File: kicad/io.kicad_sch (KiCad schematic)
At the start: 14 parts, among them P1 Mini-DIN_6pins_ver3, SW2 SW_DIP_x08, U6 74HC273, U8 74HC244

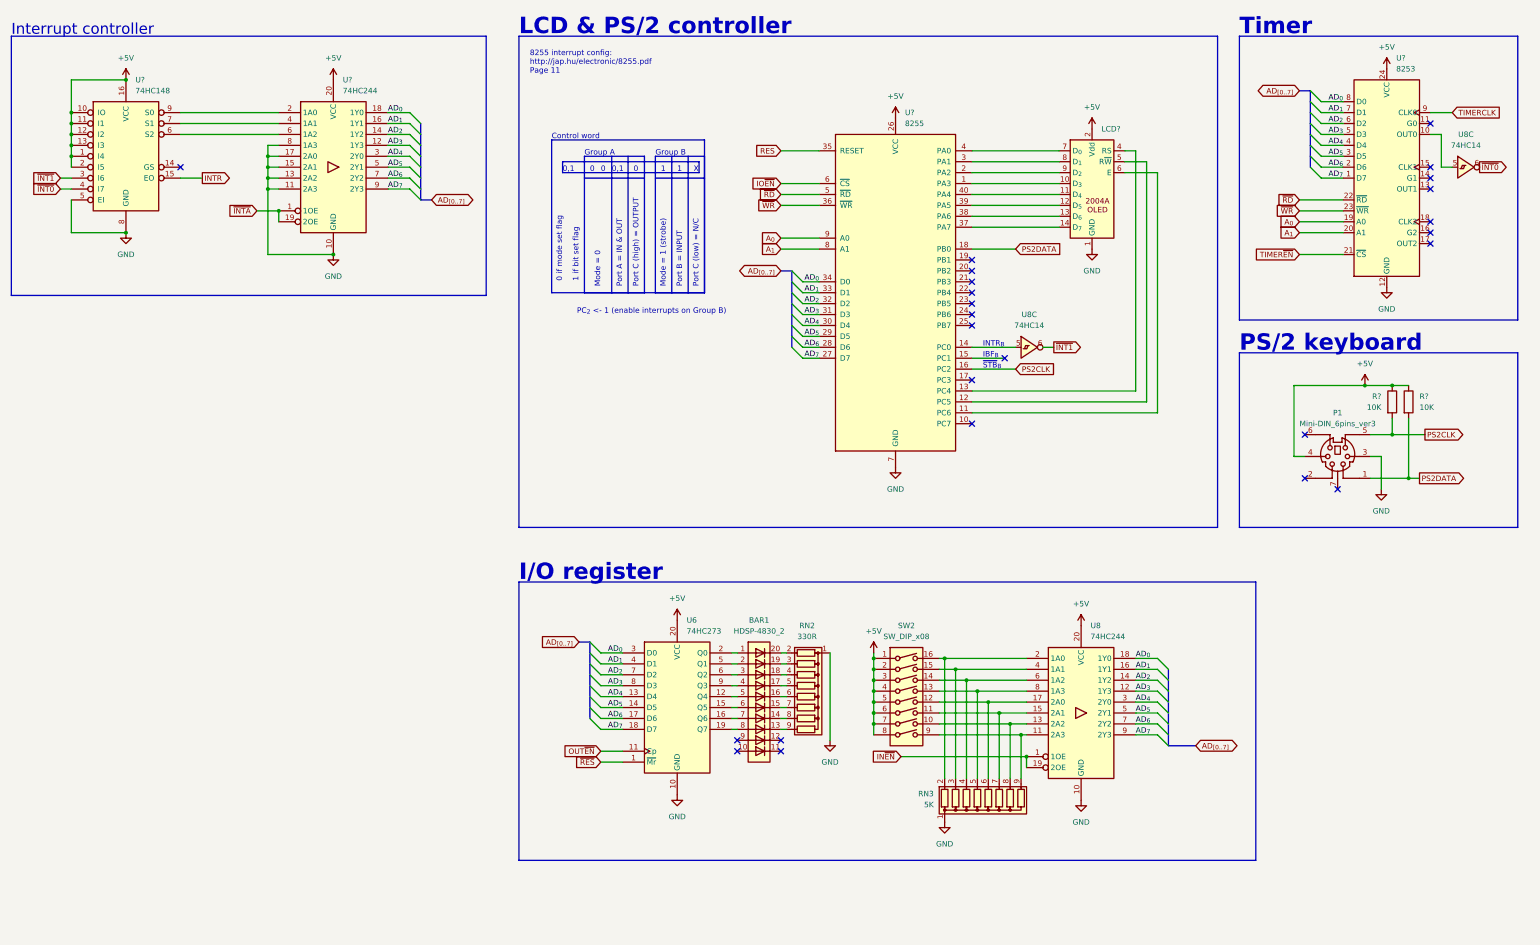
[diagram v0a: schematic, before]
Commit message: Add UART
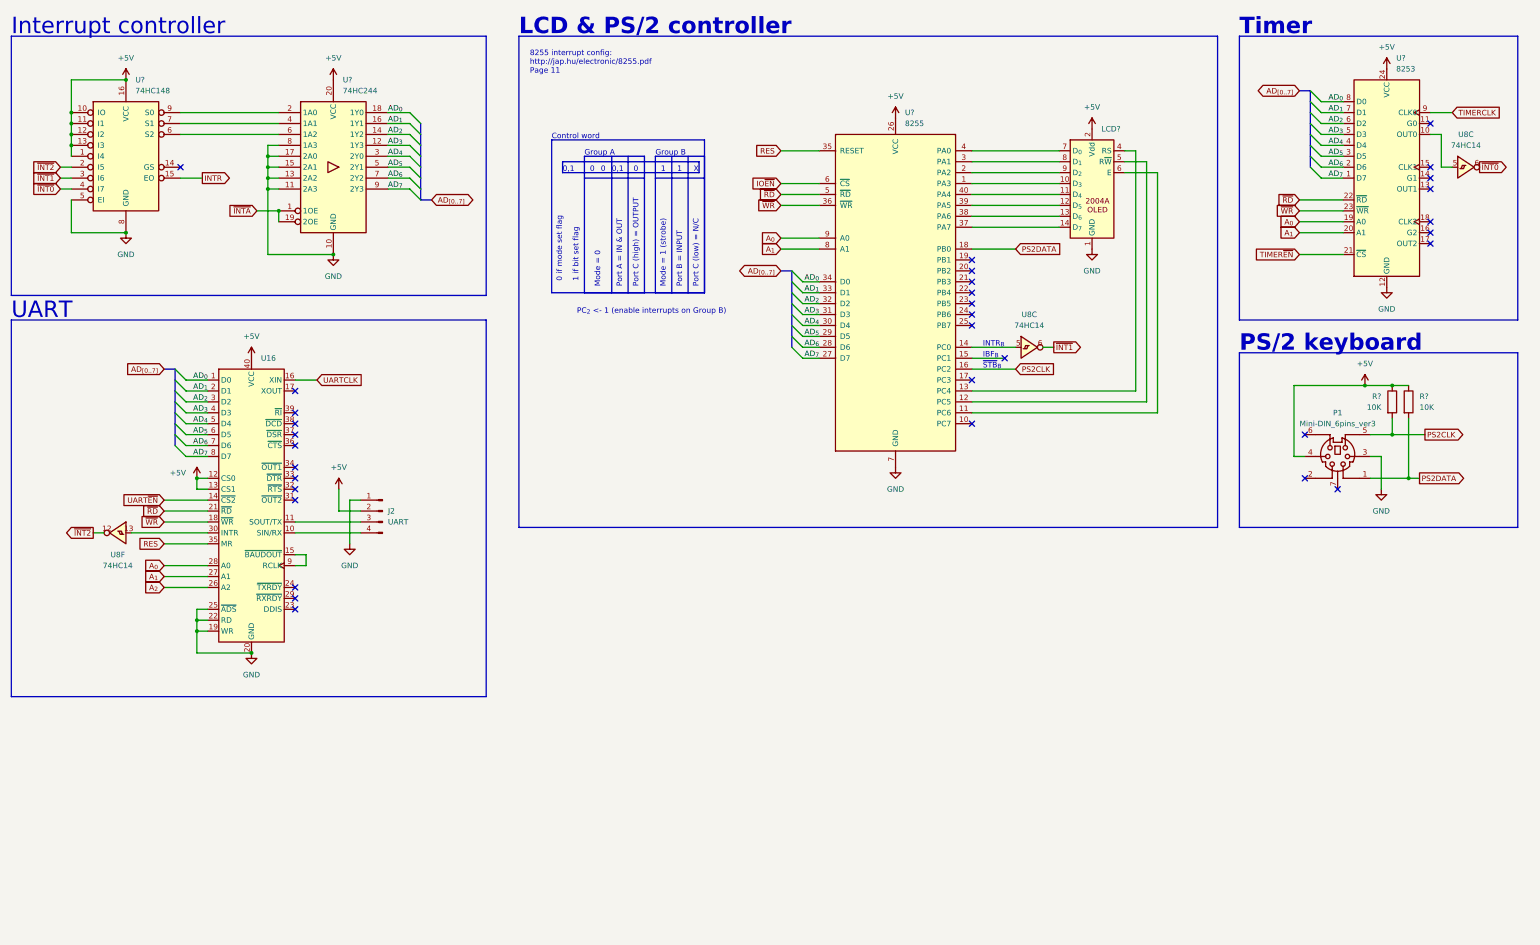
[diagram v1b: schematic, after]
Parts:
- removed BAR1: HDSP-4830_2, Display:HDSP-4830, symbol LED:HDSP-4830_2
- removed RN2: 330R, Resistor_THT:R_Array_SIP9, symbol Device:R_Network08
- removed RN3: 5K, Resistor_THT:R_Array_SIP9, symbol Device:R_Network08
- removed SW2: SW_DIP_x08, Button_Switch_THT:SW_DIP_SPSTx08_Slide_9.78x22.5mm_W7.62mm_P2.54mm, symbol Switch:SW_DIP_x08
- removed U6: 74HC273, Package_DIP:DIP-20_W7.62mm_Socket, symbol 74xx:74HC273
- removed unit 1 of U8
- added J2: UART, symbol Connector:Conn_01x04_Pin
- added U16: ~, Package_DIP:DIP-40_W15.24mm_Socket, symbol 82xx:8250/16550
- added unit 6 of U8
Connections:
- net +5V: now also J2.2 (Pin_2), U16.12 (CS0), U16.13 (CS1), U16.40 (VCC); no longer U?.2 (I5)
- net AD_{0}: now also U16.1 (D0)
- net AD_{1}: now also U16.2 (D1)
- net AD_{2}: now also U16.3 (D2)
- net AD_{3}: now also U16.4 (D3)
- net AD_{4}: now also U16.5 (D4)
- net AD_{5}: now also U16.6 (D5)
- net AD_{6}: now also U16.7 (D6)
- net AD_{7}: now also U16.8 (D7)
- net A_{0}: now also U16.28 (A0)
- net A_{1}: now also U16.27 (A1)
- net GND: now also J2.1 (Pin_1), U16.19 (WR), U16.20 (GND), U16.22 (RD), U16.25 (~{ADS})
- net RES: now also U16.35 (MR)
- net ~{RD}: now also U16.21 (~{RD})
- net ~{WR}: now also U16.18 (~{WR})
- new net: J2.4 (Pin_4), U16.10 (SIN/RX)
- new net: J2.3 (Pin_3), U16.11 (SOUT/TX)
- new net: U16.15 (~{BAUDOUT}), U16.9 (RCLK)
- new net: U16.30 (INTR), U8.13
- new net A_{2}: U16.26 (A2)
- new net UARTCLK: U16.16 (XIN)
- new net UART~{EN}: U16.14 (~{CS2})
- new net ~{INT2}: U8.12, U?.2 (I5)
- no-connect marks 25 -> 33
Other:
- note added: "UART"
- note removed: "I/O register"

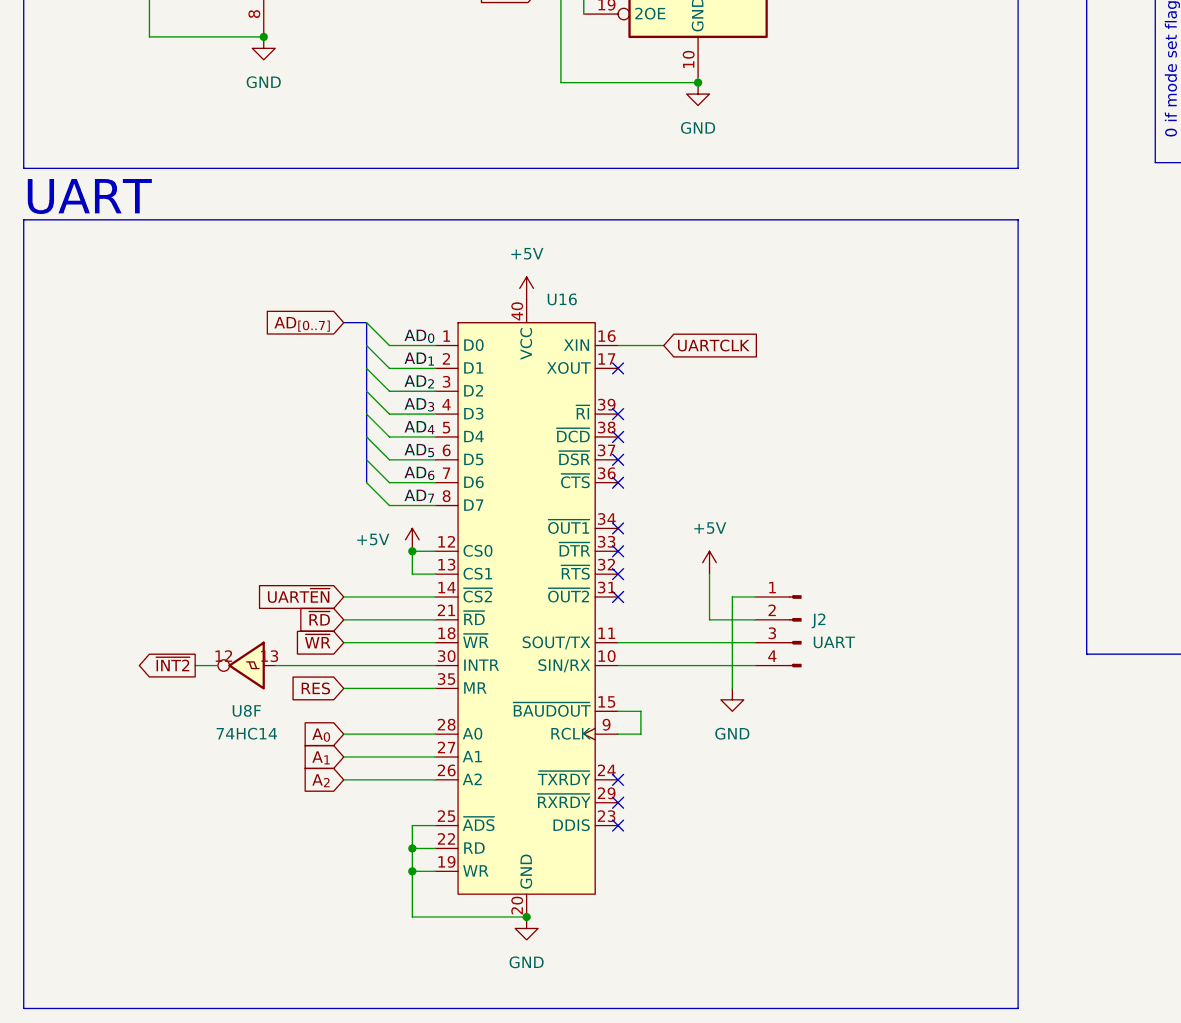
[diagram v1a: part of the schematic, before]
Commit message: Add UART & uSD card
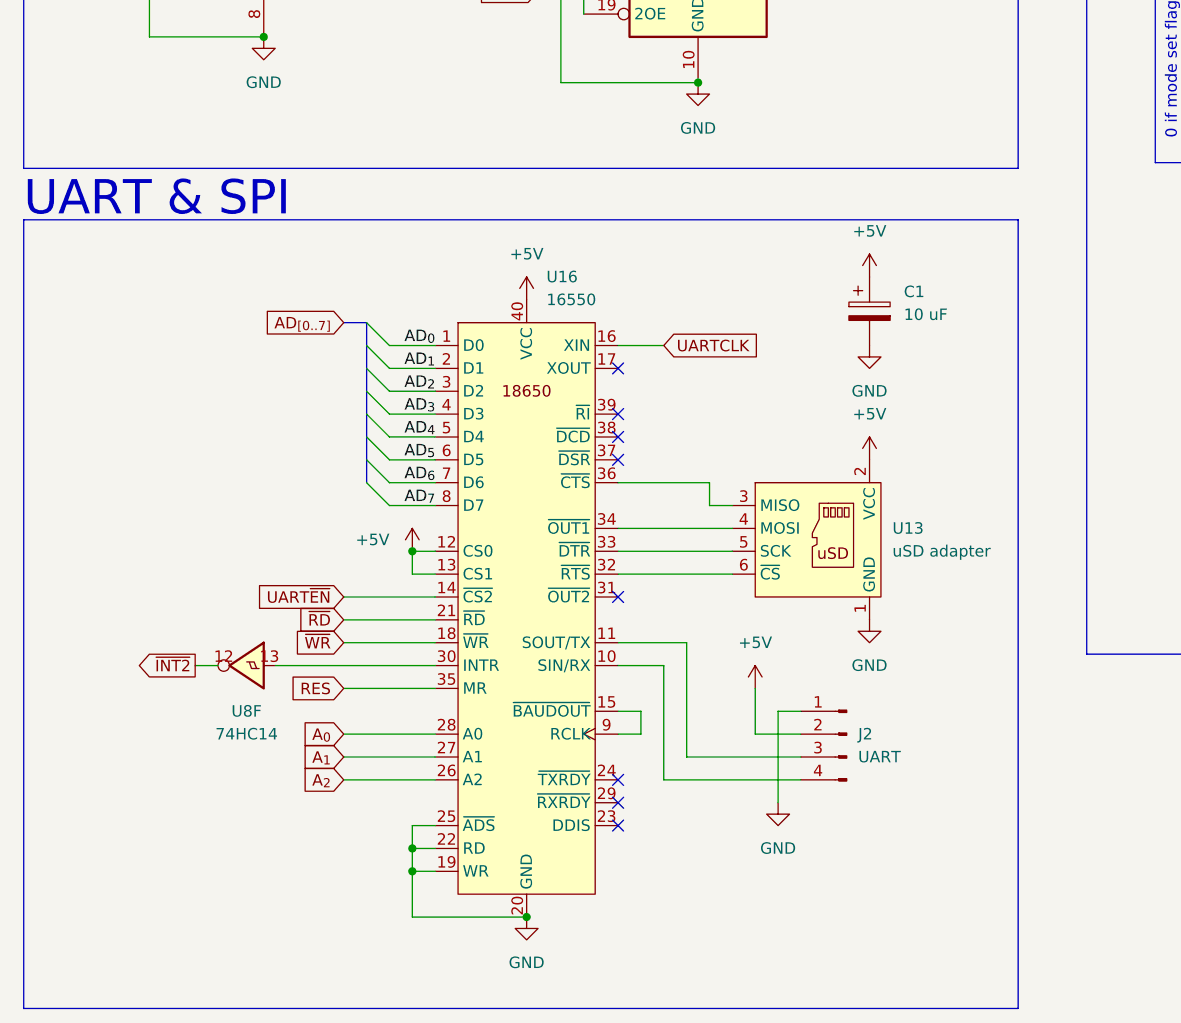
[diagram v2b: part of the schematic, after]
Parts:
- added C1: 10 uF, Capacitor_THT:CP_Radial_D6.3mm_P2.50mm, symbol Device:C_Polarized
- added U13: uSD adapter, footprints:MicroSD-Adapter, symbol my:uSD-adapter
- J2: footprint (none) -> Connector_PinHeader_2.54mm:PinHeader_1x04_P2.54mm_Vertical
- U16: value ~ -> 16550
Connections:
- net +5V: now also C1.1, U13.2 (VCC)
- net GND: now also C1.2, U13.1 (GND)
- net at U16.32 (~{RTS}): now also U13.6 (~{CS})
- net at U16.33 (~{DTR}): now also U13.5 (SCK)
- net at U16.34 (~{OUT1}): now also U13.4 (MOSI)
- net at U16.36 (~{CTS}): now also U13.3 (MISO)
- no-connect marks 33 -> 29
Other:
- note added: "UART & SPI"
- note removed: "UART"
- moved on the sheet: J2

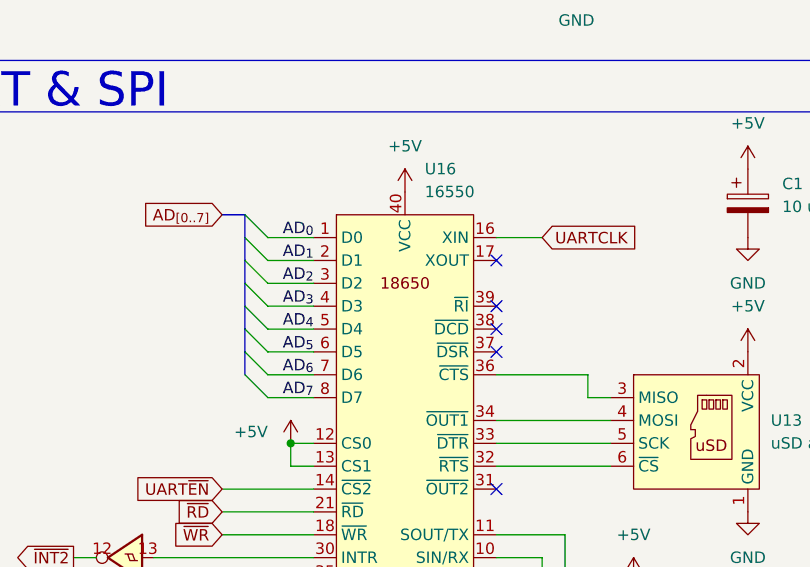
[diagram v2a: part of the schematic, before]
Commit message: Update symbols
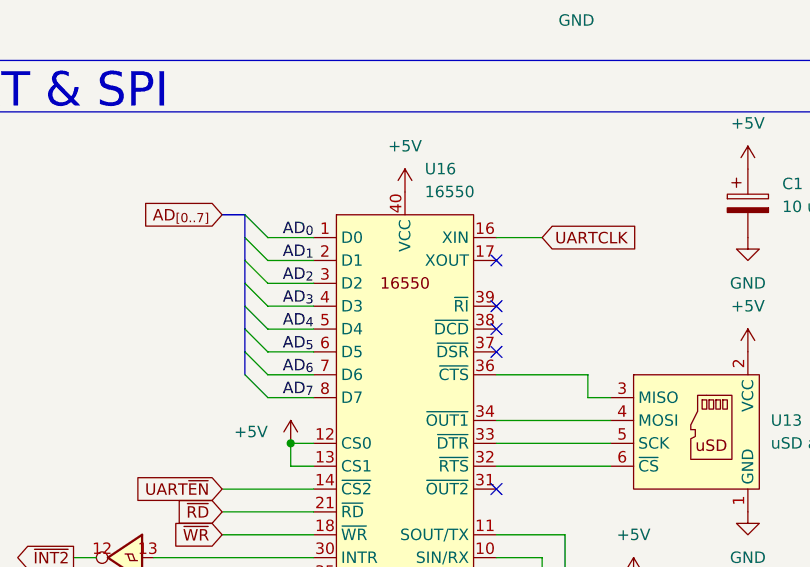
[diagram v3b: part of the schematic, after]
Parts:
- U16: symbol 82xx:8250/16550 -> 82xx:16550
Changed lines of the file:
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@@
     )
   )
-  (symbol (lib_id "82xx:8250/16550") (at 66.04 99.06 0) (unit 1)
+  (symbol (lib_id "82xx:16550") (at 66.04 99.06 0) (unit 1)
     (in_bom yes) (on_board yes) (dnp no) (fields_autoplaced)
     (property "Reference" "U16" (at 75.8541 93.98 0)

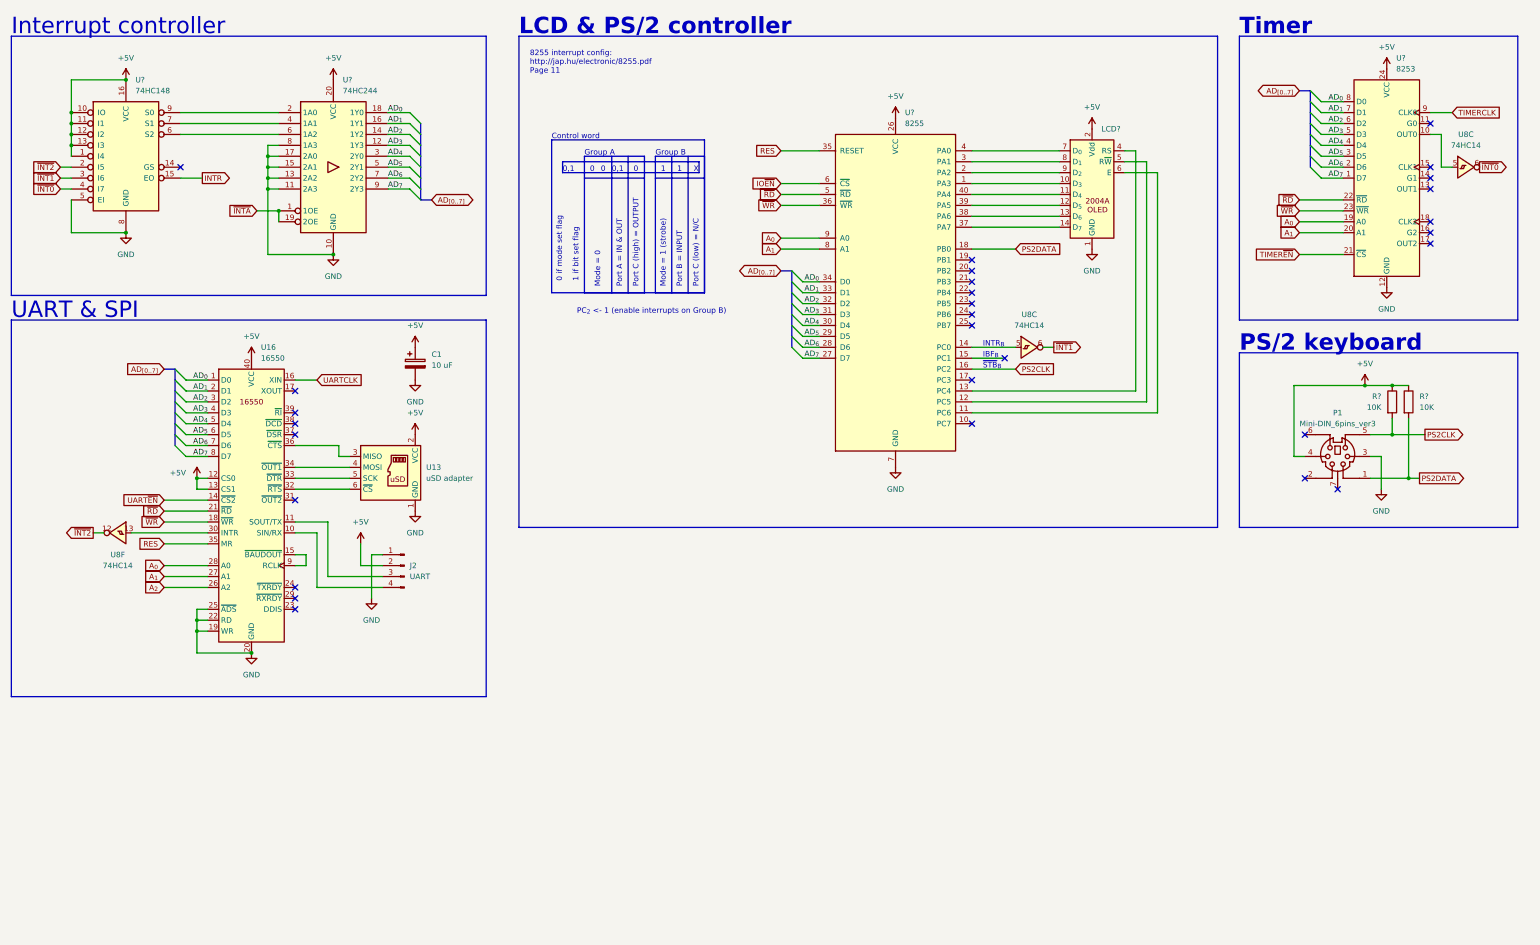
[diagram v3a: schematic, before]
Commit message: Add 8259 interrupt controller, update PCB
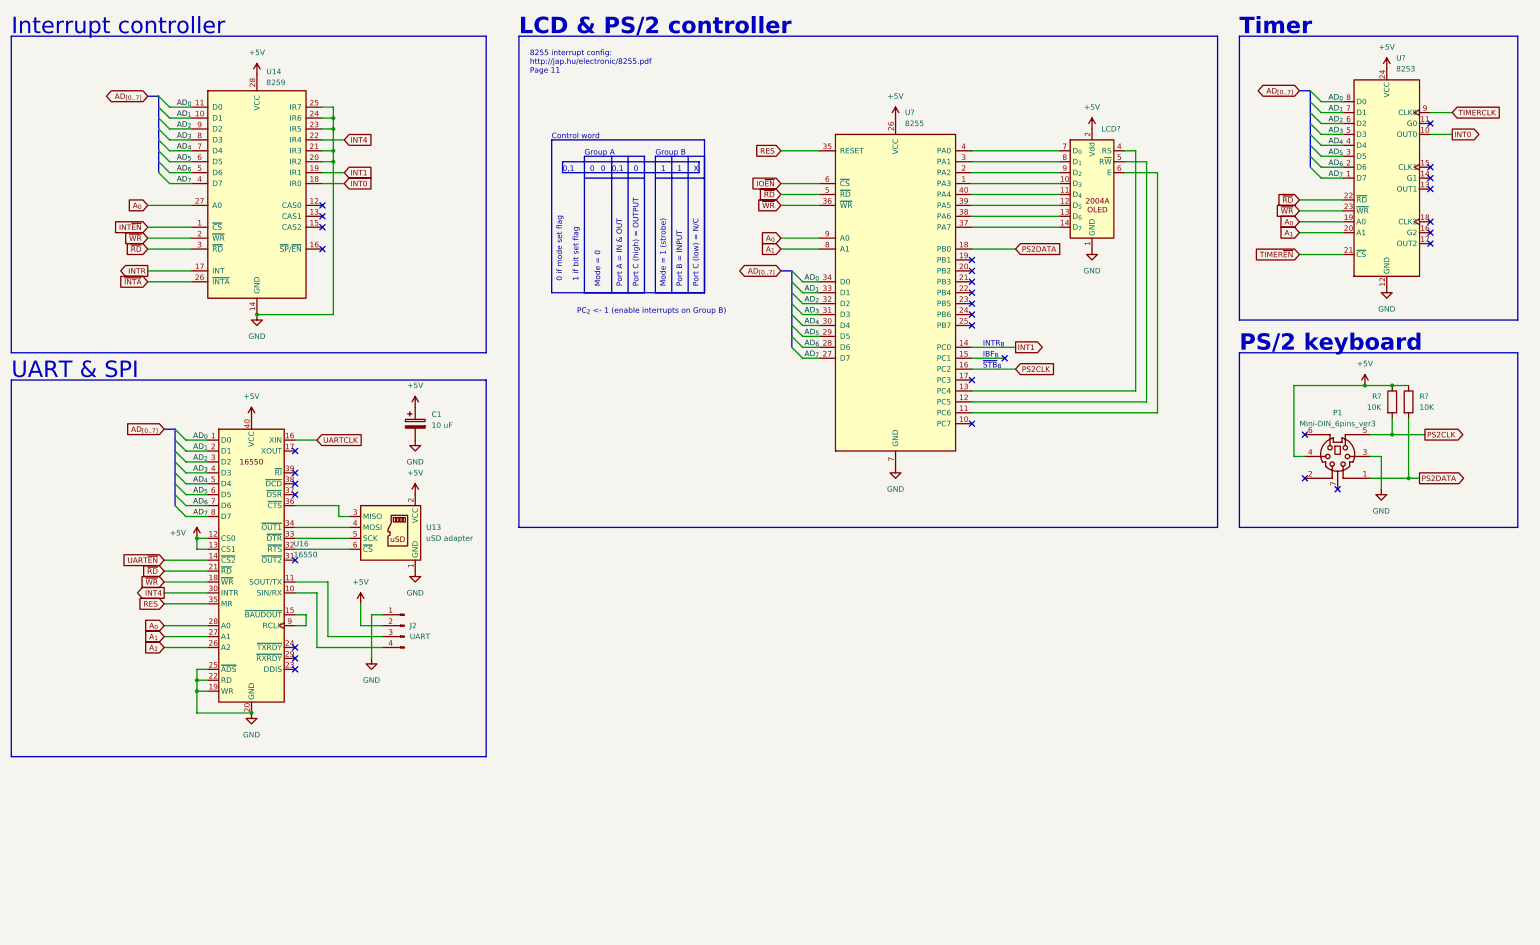
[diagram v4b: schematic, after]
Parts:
- removed U8: 74HC14, Package_DIP:DIP-14_W7.62mm_Socket, symbol 74hc00_small:74HC14_small
- removed U?: 74HC148, Package_DIP:DIP-16_W7.62mm_Socket, symbol 74xx:74LS148
- removed U?: 74HC244, Package_DIP:DIP-20_W7.62mm_Socket, symbol 74xx:74HC244
- added U14: 8259, Package_DIP:DIP-28_W15.24mm_Socket, symbol Interface:8259
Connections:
- net +5V: now also U14.28 (VCC)
- net AD_{0}: now also U14.11 (D0)
- net AD_{1}: now also U14.10 (D1)
- net AD_{2}: now also U14.9 (D2)
- net AD_{3}: now also U14.8 (D3)
- net AD_{4}: now also U14.7 (D4)
- net AD_{5}: now also U14.6 (D5)
- net AD_{6}: now also U14.5 (D6)
- net AD_{7}: now also U14.4 (D7)
- net A_{0}: now also U14.27 (A0)
- net GND: now also U14.14 (GND), U14.20 (IR2), U14.21 (IR3), U14.23 (IR5), U14.24 (IR6), U14.25 (IR7)
- net INTR: now also U14.17 (INT)
- net ~{INTA}: now also U14.26 (~{INTA})
- net ~{RD}: now also U14.3 (~{RD})
- net ~{WR}: now also U14.2 (~{WR})
- net INT4: now reaches U16.30 (INTR)
- net INT4: now also U14.22 (IR4)
- net INT0: now reaches U?.10 (OUT0)
- net INT0: now also U14.18 (IR0)
- net INT1: now reaches U?.14 (PC0)
- net INT1: now also U14.19 (IR1)
- new net INT~{EN}: U14.1 (~{CS})
- no-connect marks 29 -> 32
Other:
- moved on the sheet: C1, J2, U13, U16
